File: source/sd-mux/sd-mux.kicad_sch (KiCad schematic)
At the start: 22 parts, among them IC1 PCA9536DP,118, J1 USB_A, J2 Micro_SD_Card_Det, U1 USB2641I-HZH-02, U2 FT200XD, U4 TS3A27518EPW, U5 SD_CONNECTOR, Y1 24MHz

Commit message: switch i2c to gpio for mux, add 3v3 converter
Change-type: patch
Signed-off-by: Ryan Cooke <ryan@balena.io>
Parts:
- removed IC1: PCA9536DP,118, SOP65P490X110-8N, symbol PCA9536DP_118:PCA9536DP,118
- removed L1: 300mH, symbol pspice:INDUCTOR
- removed U2: FT200XD, Package_DFN_QFN:DFN-10-1EP_3x3mm_P0.5mm_EP1.55x2.48mm, symbol Interface_USB:FT200XD
- added C10: 1uF, symbol Device:C
- added C11, C13, C15, C16, C18, C19, C9: 4.7uF, symbol Device:C
- added C12, C14: 10uF, symbol Device:C
- added C17: 18pF, symbol Device:C
- added C8: 100nF, symbol Device:C
- added FB1, FB2: 2A/0.05DCR, symbol Device:FerriteBead
- added IC1: NCP1117DT33G, NCP1117DT33G, symbol NCP1117DT33G:NCP1117DT33G
- added IC2: FT260S-U, SOP65P640X120-28N, symbol FT260S-U:FT260S-U
- added R10: 4.7k, symbol Device:R
- added R11, R12, R8, R9: 10k, symbol Device:R
- added R13: 51k, symbol Device:R
- added R6: 12k, symbol Device:R
- C5: value 100nF -> 4.7uF
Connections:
- net GND: now also J2.11 (SHIELD), R4.1, U4.5 (GND), C10.2, C11.2, C12.2, C13.2, C14.2, C15.2, C16.2, C17.2, C18.2, C19.2, C8.2, C9.1, FB1.1, FB1.2, IC1.1 (ADJUST/GROUND), IC2.23 (GND), IC2.28 (AGND), R6.2
- net SD_CLK_HUB: now also U1.21 (SD_CLK/MS_BS)
- net SD_CMD_HUB: no longer U1.21 (SD_CLK/MS_BS)
- net SD_D2_DUT: no longer U1.33 (SD_D2)
- net SD_D2_HUB: now also U1.33 (SD_D2)
- net SD_D3_DUT: no longer U1.32 (SD_D3/MS_D3)
- net SD_D3_HUB: now also U1.32 (SD_D3/MS_D3)
- net SD_MUX_SEL: now also IC2.11 (DIO0)
- net USBDN_D_N2: now also IC2.24 (DM)
- net USBDN_D_P2: now also IC2.25 (DP)
- net VBUS: now also C10.1, C14.1, C19.1, FB2.1, FB2.2, IC1.3 (INPUT), IC2.27 (VCCIN), R13.1
- net VD33: now also C5.1, C11.1, C12.1, C13.1, C17.1, C9.2, IC1.2 (OUTPUT)
- net at J1.5 (Shield): now also C8.1, R6.1
- new net: IC2.2 (VBUS_DET), R13.2
- new net: C15.1, IC2.7 (RESETN), R10.2
- new net: IC2.5 (DEBUGGER), R12.2
- new net: IC2.6 (STEST_RSTN), R11.2
- new net: IC2.8 (DCNF0), R9.2
- new net: IC2.9 (DCNF1), R8.2
- new net VCCIO: C16.1, C18.1, IC2.10 (VCCIO), IC2.26 (VOUT3V3), R10.1, R11.1, R12.1, R8.1, R9.1
- no-connect marks 25 -> 34
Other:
- note added: "3v3 voltage regulator"
- note added: "4.7uF depcoupling capacitors recommended by datasheet"
- note added: "GPIOA pin attached to SD mux toggle Can be toggled via HID command [0xB0, X, X, 0x02, 0x02]"
- note added: "Provides 3.3V supply voltage for the USB hub"
- note added: "RC delay to pull up reset pin of USB hub"
- note added: "SD female connector"
- note added: "SD male connector"
- note added: "SDIO multiplexer"
- note added: "USB Controller"
- note added: "USB to GPIO bridge"
- note added: "Upstream USB"
- note removed: "3V3OUT pin of this chip is the output of a 3.3V LDO regulator. This is used for the 3.3V rail for the other IC's"
- note removed: "Address is fixed to 1000 001"
- note removed: "IO pins are HIGH by default"
- note removed: "IO pins are INPUTS by default They can be configured to be outputs by setting the corresponding bit in register 3 to 0"
- note removed: "RC delay to pull up reset pin"
- note removed: "This IO expander is used to drive the multiplexer IC"
- company: (none) -> balena
- title: (none) -> Autokit SD card Multiplexer
- moved on the sheet: C1, C2, C3, C4, C6, C7, J1, J2, R1, R2, R3, R4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

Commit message: fixup schematic based on reviewer comments
Change-type: patch
Signed-off-by: Ryan Cooke <ryan@balena.io>
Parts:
- removed J1: USB_A, symbol Connector:USB_A
- added C20, C21, C23, C24: 4.7uF, symbol Device:C
- added C22, C25, C26: 0.1uF, symbol Device:C
- added FB3, FB4: 2A/0.05DCR, symbol Device:FerriteBead
- added J1: USB_B_Micro, symbol Connector:USB_B_Micro
- added R14: 220, symbol Device:R
- added R15: 12k, symbol Device:R
- added R16: 10k, symbol Device:R
- C11, C13, C16, C18, C5, C9: value 4.7uF -> 0.1uF
- C6, C8: value 100nF -> 0.1uF
- R1: value 10k -> 100k
- R6: value 12k -> 330
- R7: value 12k -> 100k
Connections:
- net VDUT is gone; now on net SD_D3_DUT: U5. (VSS)
- net GND: now also C4.1, C9.2, C20.2, C21.2, C22.2, C23.2, C24.2, C25.2, C26.2, R15.2, R16.2; no longer C4.2, C9.1, FB1.1, R1.2
- net USBUP_D_N: now also J1.2 (D-)
- net USBUP_D_P: now also J1.3 (D+)
- net VBUS: now also R1.2, C23.1, C25.1; no longer C19.1, FB2.2
- net VCCIO: now also C21.1, C22.1, C24.1, C26.1; no longer C16.1, C18.1
- net VD33: now also FB3.1, FB4.1; no longer C11.1, C13.1, C5.1, C9.2, U1.12 (VDD33_2), U1.16 (VDD33_3), U1.25 (VDD33_4), U1.34 (VDD33_5), U1.39 (VBUS_DET), U1.41 (VDD33_6), U1.48 (VDD33_7), U1.5 (VDD33_1)
- net XTAL1: now also R14.2; no longer C1.1, R2.2, Y1.1
- net at C8.1, R6.1: now also J1.6 (Shield)
- net at U1.13 (GPIO6/SD_WP/MS_SCLK): now also R16.1; no longer R1.1
- net at U1.47 (RBIAS): now also R15.1; no longer R7.1
- net at U1.15 (CRFILT): now also C4.2; no longer C4.1
- net NRESET renamed nRESET
- net nRESET: no longer C6.1
- new net: C1.1, R14.1, R2.2, Y1.1
- new net: C11.1, C16.1, C19.1, C6.1, FB3.2, U1.41 (VDD33_6), U1.48 (VDD33_7), U1.5 (VDD33_1)
- new net: C13.1, C18.1, C20.1, C5.1, C9.1, FB4.2, U1.12 (VDD33_2), U1.16 (VDD33_3), U1.25 (VDD33_4), U1.34 (VDD33_5)
- new net: FB1.1, J1.5 (GND)
- new net: FB2.2, J1.1 (VBUS)
- new net VBUS_DET: R1.1, R7.1, U1.39 (VBUS_DET)
- no-connect marks 34 -> 37
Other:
- note added: "3v3 voltage LDO"
- note added: "Voltage from DUT SD card slot"
- note removed: "3v3 voltage regulator"
- note removed: "4.7uF depcoupling capacitors recommended by datasheet"
- moved on the sheet: C1, C10, C12, C14, C2, C7, IC1, J2, R2, R3, R5, U5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

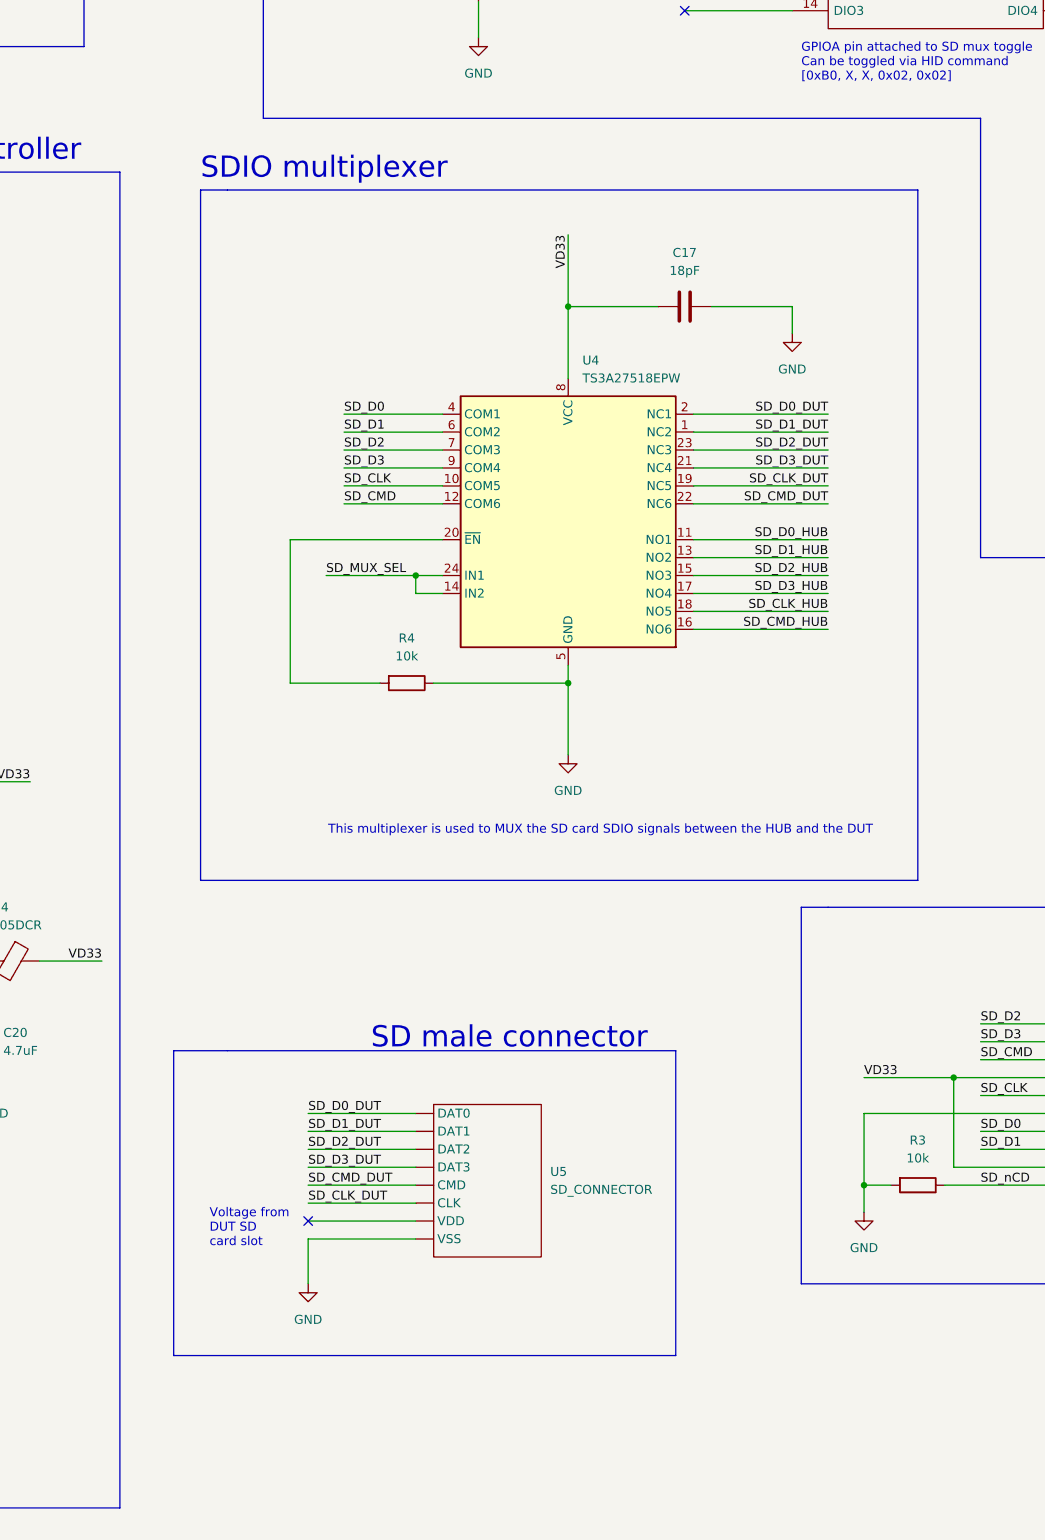
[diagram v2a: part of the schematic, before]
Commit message: add LEDs and footprints
Change-type: patch
Signed-off-by: Ryan Cooke <ryan@balena.io>
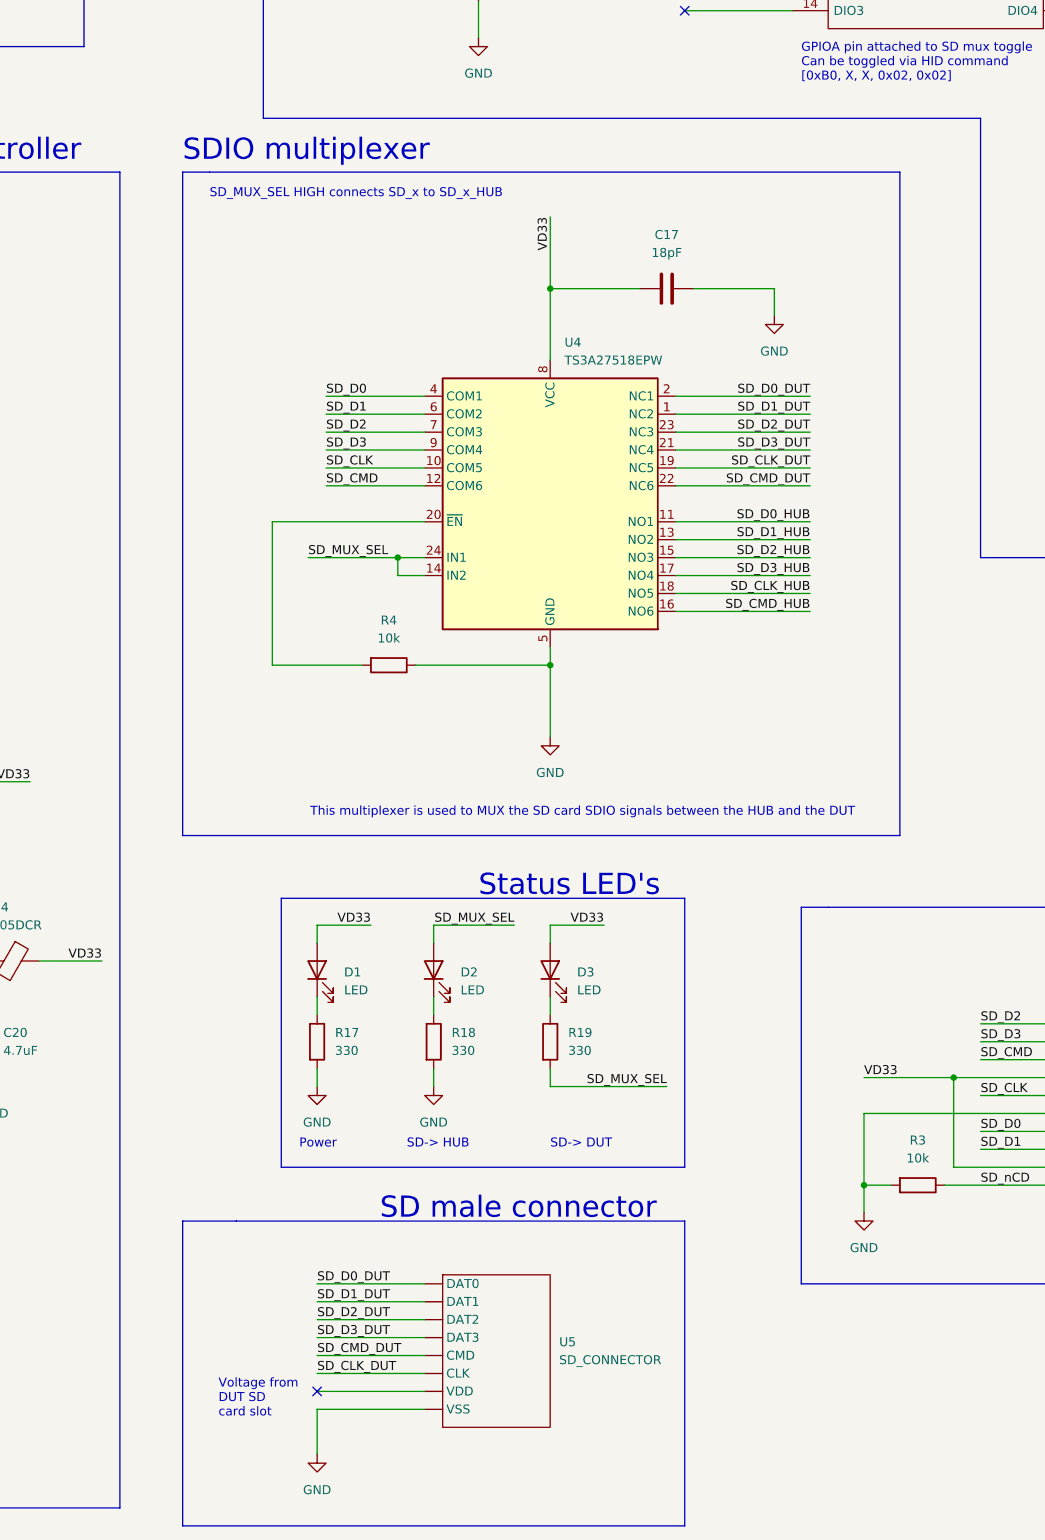
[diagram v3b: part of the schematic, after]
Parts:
- added D1, D2, D3: LED, LED_SMD:LED_0201_0603Metric, symbol Device:LED
- added R17, R18, R19: 330, Resistor_SMD:R_0201_0603Metric, symbol Device:R
- C1, C10, C11, C12, C13, C14, C15, C16, C17, C18, C19, C2, C20, C21, C22, C23, C24, C25, C26, C3, C4, C5, C6, C7, C8, C9: footprint (none) -> Capacitor_SMD:C_0201_0603Metric
- FB1, FB2, FB3, FB4: footprint (none) -> Ferrite_THT:LairdTech_28C0236-0JW-10
- J1: footprint (none) -> Connector_USB:USB_Micro-B_Wuerth_629105150521_CircularHoles
- R1, R10, R11, R12, R13, R14, R15, R16, R2, R3, R4, R5, R6, R7, R8, R9: footprint (none) -> Resistor_SMD:R_0201_0603Metric
- Y1: footprint (none) -> Crystal:Resonator_SMD_Murata_CSTxExxV-3Pin_3.0x1.1mm
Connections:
- net GND: now also R17.2, R18.2
- net SD_MUX_SEL: now also D2.2 (A), R19.2
- net VD33: now also D1.2 (A), D3.2 (A)
- new net: D2.1 (K), R18.1
- new net: D1.1 (K), R17.1
- new net: D3.1 (K), R19.1
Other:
- note added: "Power"
- note added: "SD-> DUT"
- note added: "SD-> HUB"
- note added: "SD_MUX_SEL HIGH connects SD_x to SD_x_HUB"
- note added: "Status LED's"
- moved on the sheet: C17, R4, U4, U5

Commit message: add pcb layout
Change-type: patch
Signed-off-by: Ryan Cooke <ryan@balena.io>
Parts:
- FB1, FB2, FB3, FB4: footprint Ferrite_THT:LairdTech_28C0236-0JW-10 -> Resistor_SMD:R_0201_0603Metric
- J2: footprint (none) -> Connector_Card:microSD_HC_Molex_104031-0811
- U5: footprint (none) -> SD:SD_connector
- Y1: footprint Crystal:Resonator_SMD_Murata_CSTxExxV-3Pin_3.0x1.1mm -> Crystal:Crystal_SMD_2016-4Pin_2.0x1.6mm
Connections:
- net GND: now also U5.6 (VSS); no longer U5. (VSS)
- net SD_CLK_DUT: now also U5.5 (CLK); no longer U5. (VSS)
- net SD_CMD_DUT: now also U5.3 (CMD); no longer U5. (VSS)
- net SD_D0_DUT: now also U5.7 (DAT0); no longer U5. (VSS)
- net SD_D1_DUT: now also U5.8 (DAT1); no longer U5. (VSS)
- net SD_D2_DUT: now also U5.1 (DAT2); no longer U5. (VSS)
- net SD_D3_DUT: now also U5.2 (DAT3); no longer U5. (VSS)
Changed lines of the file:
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@@
     (stroke (width 0) (type default) (color 0 0 0 0))
   )
-  (wire (pts (xy 190.5 39.37) (xy 195.58 39.37))
-    (stroke (width 0) (type default) (color 0 0 0 0))
-  )
   (wire (pts (xy 167.64 219.71) (xy 180.34 219.71))
     (stroke (width 0) (type default) (color 0 0 0 0))
@@
     (stroke (width 0) (type default) (color 0 0 0 0))
   )
+  (wire (pts (xy 190.5 39.37) (xy 195.58 39.37))
+    (stroke (width 0) (type default) (color 0 0 0 0))
+  )
   (wire (pts (xy 134.62 212.09) (xy 134.62 214.63))
     (stroke (width 0) (type default) (color 0 0 0 0))
@@
       (effects (font (size 1.27 1.27)) (justify left))
     )
-    (property "Footprint" "Ferrite_THT:LairdTech_28C0236-0JW-10" (id 2) (at 198.12 201.422 90)
+    (property "Footprint" "Resistor_SMD:R_0201_0603Metric" (id 2) (at 198.12 201.422 90)
       (effects (font (size 1.27 1.27)) hide)
     )
@@
     (property "Reference" "J2" (id 0) (at 368.935 200.66 0))
     (property "Value" "Micro_SD_Card_Det" (id 1) (at 368.935 203.2 0))
-    (property "Footprint" "" (id 2) (at 420.37 204.47 0)
+    (property "Footprint" "Connector_Card:microSD_HC_Molex_104031-0811" (id 2) (at 420.37 204.47 0)
       (effects (font (size 1.27 1.27)) hide)
     )
@@
     (property "Reference" "Y1" (id 0) (at 72.39 236.22 0))
     (property "Value" "24MHz" (id 1) (at 72.39 238.76 0))
-    (property "Footprint" "Crystal:Resonator_SMD_Murata_CSTxExxV-3Pin_3.0x1.1mm" (id 2) (at 72.39 243.84 0)
+    (property "Footprint" "Crystal:Crystal_SMD_2016-4Pin_2.0x1.6mm" (id 2) (at 72.39 243.84 0)
       (effects (font (size 1.27 1.27)) hide)
     )
@@
       (effects (font (size 1.27 1.27)) (justify left))
     )
-    (property "Footprint" "" (id 2) (at 266.7 242.57 0)
+    (property "Footprint" "SD:SD_connector" (id 2) (at 266.7 242.57 0)
       (effects (font (size 1.27 1.27)) hide)
     )
@@
       (effects (font (size 1.27 1.27)) hide)
     )
-    (pin "")
-    (pin "")
-    (pin "")
-    (pin "")
-    (pin "")
-    (pin "")
-    (pin "")
-    (pin "")
+    (pin "5")
+    (pin "3")
+    (pin "7")
+    (pin "8")
+    (pin "1")
+    (pin "2")
+    (pin "4")
+    (pin "6")
   )
   (symbol (lib_id "Device:FerriteBead") (at 59.69 62.23 0) (unit 1)
@@
       (effects (font (size 1.27 1.27)) (justify left))
     )
-    (property "Footprint" "Ferrite_THT:LairdTech_28C0236-0JW-10" (id 2) (at 57.912 62.23 90)
+    (property "Footprint" "Resistor_SMD:R_0201_0603Metric" (id 2) (at 57.912 62.23 90)
       (effects (font (size 1.27 1.27)) hide)
     )
@@
   )
   (symbol (lib_id "NCP1117DT33G:NCP1117DT33G") (at 158.75 40.64 0) (unit 1)
-    (in_bom yes) (on_board yes) (fields_autoplaced)
+    (in_bom yes) (on_board yes)
     (property "Reference" "IC1" (id 0) (at 168.91 31.75 0))
     (property "Value" "NCP1117DT33G" (id 1) (at 168.91 34.29 0))
-    (property "Footprint" "NCP1117DT33G" (id 2) (at 198.12 38.1 0)
-      (effects (font (size 1.27 1.27)) (justify left) hide)
+    (property "Footprint" "NCP1117DT33G" (id 2) (at 171.45 45.72 0)
+      (effects (font (size 1.27 1.27)) (justify left))
     )
     (property "Datasheet" "https://www.onsemi.com/pdf/datasheet/ncp1117-d.pdf" (id 3) (at 198.12 40.64 0)
@@
       (effects (font (size 1.27 1.27)) (justify left))
     )
-    (property "Footprint" "Ferrite_THT:LairdTech_28C0236-0JW-10" (id 2) (at 82.55 33.782 90)
+    (property "Footprint" "Resistor_SMD:R_0201_0603Metric" (id 2) (at 82.55 33.782 90)
       (effects (font (size 1.27 1.27)) hide)
     )
@@
       (effects (font (size 1.27 1.27)) (justify left))
     )
-    (property "Footprint" "Ferrite_THT:LairdTech_28C0236-0JW-10" (id 2) (at 186.69 176.022 90)
+    (property "Footprint" "Resistor_SMD:R_0201_0603Metric" (id 2) (at 186.69 176.022 90)
       (effects (font (size 1.27 1.27)) hide)
     )
@@
     )
     (path "/a69c5889-ac1c-4f38-8955-eb3e6c187e3f"
-      (reference "FB1") (unit 1) (value "2A/0.05DCR") (footprint "Ferrite_THT:LairdTech_28C0236-0JW-10")
+      (reference "FB1") (unit 1) (value "2A/0.05DCR") (footprint "Resistor_SMD:R_0201_0603Metric")
     )
     (path "/d0fbdc20-e8de-413d-b999-f10b886e0d01"
-      (reference "FB2") (unit 1) (value "2A/0.05DCR") (footprint "Ferrite_THT:LairdTech_28C0236-0JW-10")
+      (reference "FB2") (unit 1) (value "2A/0.05DCR") (footprint "Resistor_SMD:R_0201_0603Metric")
     )
     (path "/e232bb16-6383-4260-abe5-04511c6231c6"
-      (reference "FB3") (unit 1) (value "2A/0.05DCR") (footprint "Ferrite_THT:LairdTech_28C0236-0JW-10")
+      (reference "FB3") (unit 1) (value "2A/0.05DCR") (footprint "Resistor_SMD:R_0201_0603Metric")
     )
     (path "/59affe93-7816-4090-8546-2b146ddc1d5a"
-      (reference "FB4") (unit 1) (value "2A/0.05DCR") (footprint "Ferrite_THT:LairdTech_28C0236-0JW-10")
+      (reference "FB4") (unit 1) (value "2A/0.05DCR") (footprint "Resistor_SMD:R_0201_0603Metric")
     )
     (path "/a81a2dad-f917-417a-a540-2d334f0ac69e"
@@
     )
     (path "/6d0d7f1e-b94b-4e88-aab5-d2db898579cd"
-      (reference "J2") (unit 1) (value "Micro_SD_Card_Det") (footprint "")
+      (reference "J2") (unit 1) (value "Micro_SD_Card_Det") (footprint "Connector_Card:microSD_HC_Molex_104031-0811")
     )
     (path "/32ef3151-e0f5-4760-9822-de934962feb8"
@@
     )
     (path "/a5f34429-e2ed-4c30-8fb9-6d6d08ef4e3f"
-      (reference "U5") (unit 1) (value "SD_CONNECTOR") (footprint "")
+      (reference "U5") (unit 1) (value "SD_CONNECTOR") (footprint "SD:SD_connector")
     )
     (path "/a16cfd73-6e44-4daf-ab2b-01b13a9b1e74"
-      (reference "Y1") (unit 1) (value "24MHz") (footprint "Crystal:Resonator_SMD_Murata_CSTxExxV-3Pin_3.0x1.1mm")
+      (reference "Y1") (unit 1) (value "24MHz") (footprint "Crystal:Crystal_SMD_2016-4Pin_2.0x1.6mm")
     )
   )
